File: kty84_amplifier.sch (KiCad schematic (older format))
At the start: 0 parts

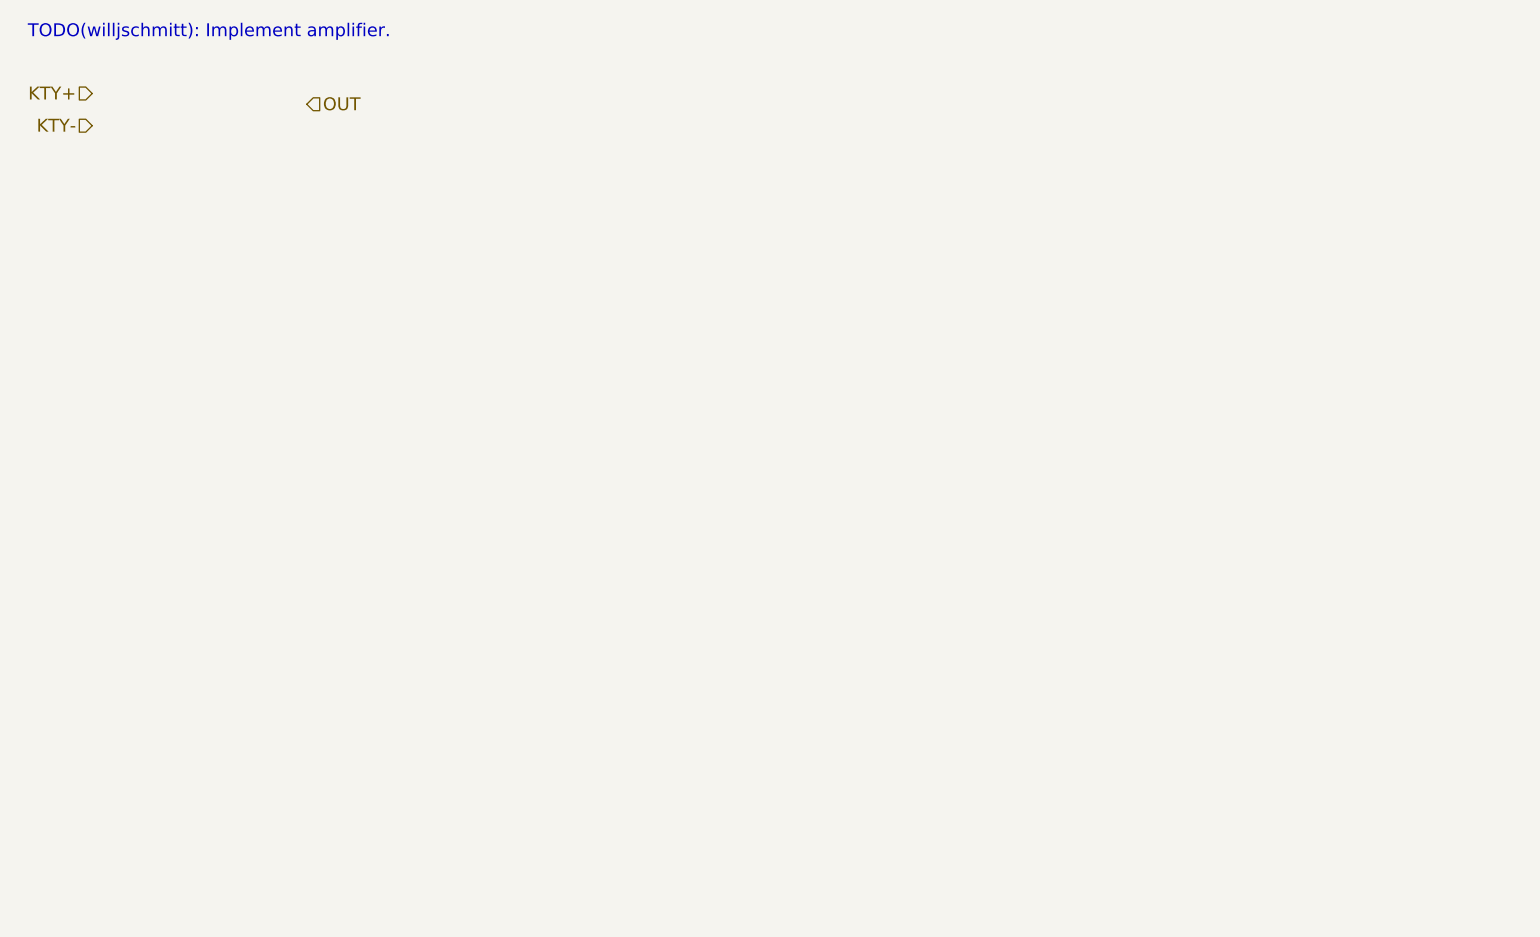
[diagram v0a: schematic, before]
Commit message: Implement temperature sensor amplifier.
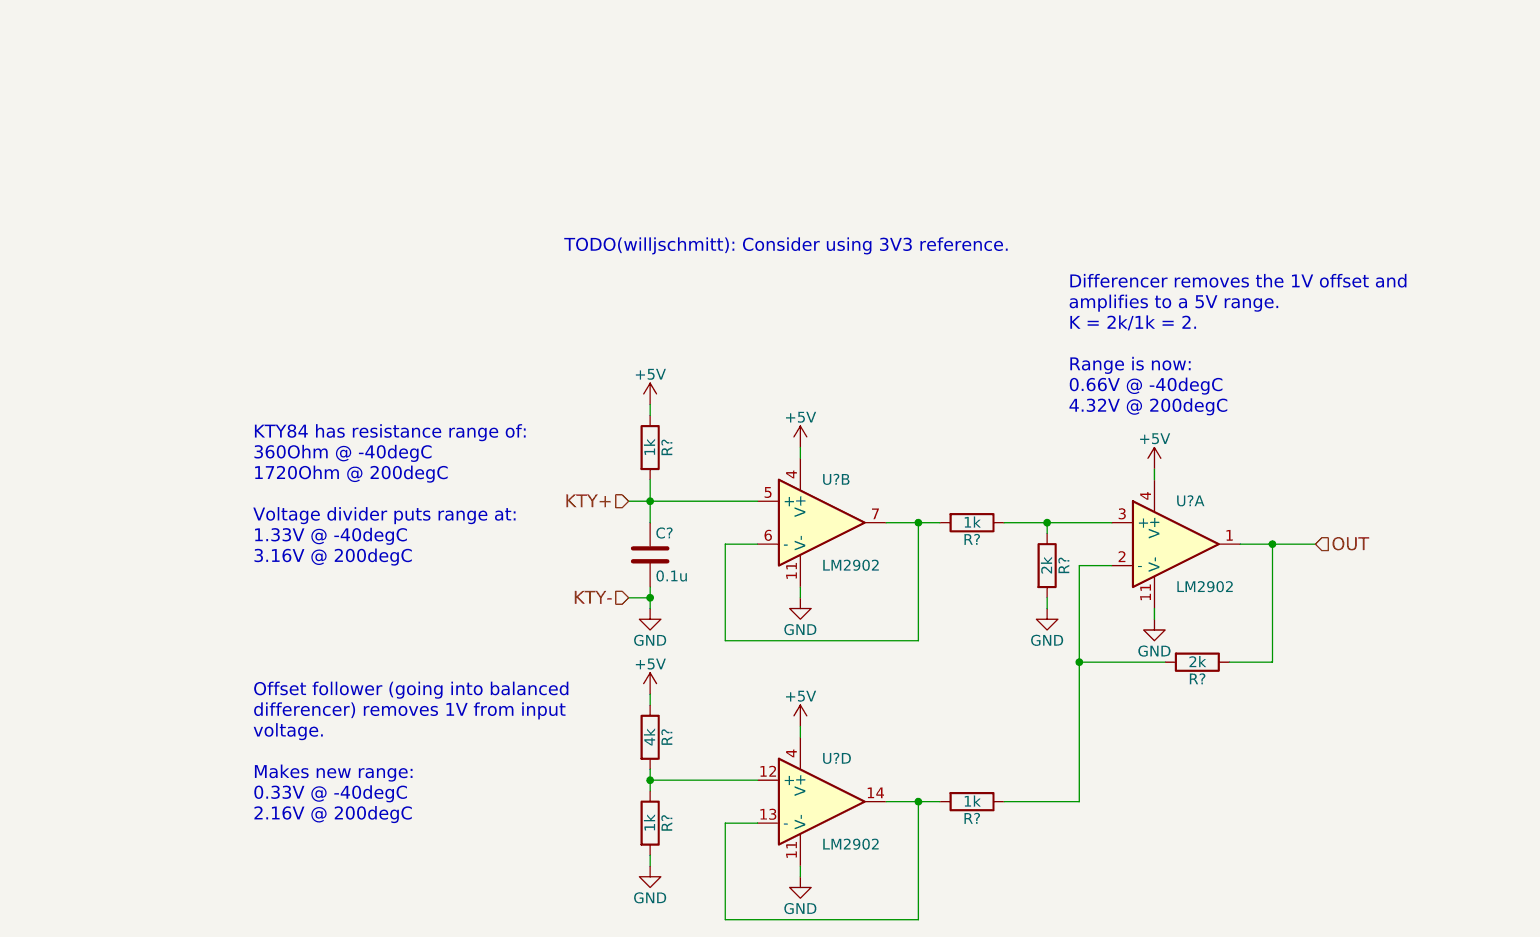
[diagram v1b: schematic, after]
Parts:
- added C?: 0.1u, symbol C
- added R? (x4): 1k, symbol R
- added R?: 4k, symbol R
- added R? (x2): 2k, symbol R
- added U? (x3): LM2902, symbol LM2902
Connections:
- net KTY+: now also C?.1, R?.2, U?.5 (+)
- net OUT: now also R?.1, U?.1
- new net: R?.1, R?.2, U?.2 (-)
- new net: R?.1, R?.1, U?.3 (+)
- new net: R?.2, U?.6 (-), U?.7
- new net: R?.1, R?.2, U?.12 (+)
- new net: R?.2, U?.13 (-), U?.14
- new net +5V: R?.1, R?.1, U?.4 (V+), U?.4 (V+), U?.4 (V+)
- new net GND: C?.2, R?.2, R?.2, U?.11 (V-), U?.11 (V-), U?.11 (V-)
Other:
- note added: "Differencer removes the 1V offset and\namplifies to a 5V range.\nK = 2k/1k = 2.\n\nRange is now:\n0.66V @ -40degC\n4.32V @ 200degC"
- note added: "KTY84 has resistance range of:\n360Ohm @ -40degC\n1720Ohm @ 200degC\n\nVoltage divider puts range at:\n1.33V @ -40degC\n3.16V @ 200degC"
- note added: "Offset follower (going into balanced\ndifferencer) removes 1V from input\nvoltage.\n\nMakes new range:\n0.33V @ -40degC\n2.16V @ 200degC\n"
- note added: "TODO(willjschmitt): Consider using 3V3 reference."
- note removed: "TODO(willjschmitt): Implement amplifier."

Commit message: Annotate and add negative IOC faults.
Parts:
- gave numbers to parts that had none: 9
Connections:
- net KTY+: now also U9.12 (+); no longer U9.5 (+)
- net OUT: now also U9.7; no longer U9.1
- net at R13.1, R15.2: now also U9.6 (-); no longer U9.2 (-)
- net at R12.1, R14.1: now also U9.5 (+); no longer U9.3 (+)
- net at R10.2, R11.1: now also U9.3 (+); no longer U9.12 (+)
- new net: R12.2, U9.13 (-), U9.14
- new net: R13.2, U9.1, U9.2 (-)
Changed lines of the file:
@@
 TODO(willjschmitt): Consider using 3V3 reference.
 $Comp
-L LM2902 U?
-U 1 1 5B0174FE
+L LM2902 U9
+U 2 1 5B0174FE
 P 7200 3400
-F 0 "U?" H 7200 3600 50  0000 L CNN
+AR Path="/5AF6F00C/5B0174FE" Ref="U9"  Part="3"
+AR Path="/5AF71A27/5B0174FE" Ref="U10"  Part="2"
+F 0 "U10" H 7200 3600 50  0000 L CNN
 F 1 "LM2902" H 7200 3200 50  0000 L CNN
 F 2 "" H 7150 3500 50  0001 C CNN
 F 3 "" H 7250 3600 50  0001 C CNN
-	1    7200 3400
-	1    0    0    -1
-$EndComp
-$Comp
-L R R?
+	2    7200 3400
+	1    0    0    -1
+$EndComp
+$Comp
+L R R9
 U 1 1 5B017561
 P 4750 2950
-F 0 "R?" V 4830 2950 50  0000 C CNN
+AR Path="/5AF6F00C/5B017561" Ref="R9"  Part="1"
+AR Path="/5AF71A27/5B017561" Ref="R16"  Part="1"
+F 0 "R16" V 4830 2950 50  0000 C CNN
 F 1 "1k" V 4750 2950 50  0000 C CNN
 F 2 "" V 4680 2950 50  0001 C CNN
@@
 $EndComp
 $Comp
-L C C?
+L C C9
 U 1 1 5B01759E
 P 4750 3450
-F 0 "C?" H 4775 3550 50  0000 L CNN
+AR Path="/5AF6F00C/5B01759E" Ref="C9"  Part="1"
+AR Path="/5AF71A27/5B01759E" Ref="C10"  Part="1"
+F 0 "C10" H 4775 3550 50  0000 L CNN
 F 1 "0.1u" H 4775 3350 50  0000 L CNN
 F 2 "" H 4788 3300 50  0001 C CNN
@@
 $EndComp
 $Comp
-L LM2902 U?
-U 2 1 5B017704
+L LM2902 U9
+U 4 1 5B017704
 P 5550 3300
-F 0 "U?" H 5550 3500 50  0000 L CNN
+AR Path="/5AF6F00C/5B017704" Ref="U9"  Part="1"
+AR Path="/5AF71A27/5B017704" Ref="U9"  Part="4"
+F 0 "U9" H 5550 3500 50  0000 L CNN
 F 1 "LM2902" H 5550 3100 50  0000 L CNN
 F 2 "" H 5500 3400 50  0001 C CNN
 F 3 "" H 5600 3500 50  0001 C CNN
-	2    5550 3300
-	1    0    0    -1
-$EndComp
-$Comp
-L LM2902 U?
-U 4 1 5B01779A
+	4    5550 3300
+	1    0    0    -1
+$EndComp
+$Comp
+L LM2902 U9
+U 1 1 5B01779A
 P 5550 4600
-F 0 "U?" H 5550 4800 50  0000 L CNN
+AR Path="/5AF6F00C/5B01779A" Ref="U9"  Part="2"
+AR Path="/5AF71A27/5B01779A" Ref="U10"  Part="1"
+F 0 "U10" H 5550 4800 50  0000 L CNN
 F 1 "LM2902" H 5550 4400 50  0000 L CNN
 F 2 "" H 5500 4700 50  0001 C CNN
 F 3 "" H 5600 4800 50  0001 C CNN
-	4    5550 4600
+	1    5550 4600
 	1    0    0    -1
 $EndComp
@@
 	5100 4700 5250 4700
 $Comp
-L R R?
+L R R10
 U 1 1 5B017B38
 P 4750 4300
-F 0 "R?" V 4830 4300 50  0000 C CNN
+AR Path="/5AF6F00C/5B017B38" Ref="R10"  Part="1"
+AR Path="/5AF71A27/5B017B38" Ref="R17"  Part="1"
+F 0 "R17" V 4830 4300 50  0000 C CNN
 F 1 "4k" V 4750 4300 50  0000 C CNN
 F 2 "" V 4680 4300 50  0001 C CNN
@@
 $EndComp
 $Comp
-L R R?
+L R R11
 U 1 1 5B017B7D
 P 4750 4700
-F 0 "R?" V 4830 4700 50  0000 C CNN
+AR Path="/5AF6F00C/5B017B7D" Ref="R11"  Part="1"
+AR Path="/5AF71A27/5B017B7D" Ref="R18"  Part="1"
+F 0 "R18" V 4830 4700 50  0000 C CNN
 F 1 "1k" V 4750 4700 50  0000 C CNN
 F 2 "" V 4680 4700 50  0001 C CNN
@@
 Connection ~ 4750 4500
 $Comp
-L GND #PWR?
+L GND #PWR54
 U 1 1 5B017EE0
 P 4750 4900
-F 0 "#PWR?" H 4750 4650 50  0001 C CNN
+AR Path="/5AF6F00C/5B017EE0" Ref="#PWR54"  Part="1"
+AR Path="/5AF71A27/5B017EE0" Ref="#PWR65"  Part="1"
+F 0 "#PWR65" H 4750 4650 50  0001 C CNN
 F 1 "GND" H 4750 4750 50  0000 C CNN
 F 2 "" H 4750 4900 50  0001 C CNN
@@
 	4750 4100 4750 4150
 $Comp
-L +5V #PWR?
+L +5V #PWR53
 U 1 1 5B019FF3
 P 4750 4100
-F 0 "#PWR?" H 4750 3950 50  0001 C CNN
+AR Path="/5AF6F00C/5B019FF3" Ref="#PWR53"  Part="1"
+AR Path="/5AF71A27/5B019FF3" Ref="#PWR64"  Part="1"
+F 0 "#PWR64" H 4750 3950 50  0001 C CNN
 F 1 "+5V" H 4750 4240 50  0000 C CNN
 F 2 "" H 4750 4100 50  0001 C CNN
@@
 $EndComp
 $Comp
-L GND #PWR?
+L GND #PWR52
 U 1 1 5B01A29C
 P 4750 3700
-F 0 "#PWR?" H 4750 3450 50  0001 C CNN
+AR Path="/5AF6F00C/5B01A29C" Ref="#PWR52"  Part="1"
+AR Path="/5AF71A27/5B01A29C" Ref="#PWR63"  Part="1"
+F 0 "#PWR63" H 4750 3450 50  0001 C CNN
 F 1 "GND" H 4750 3550 50  0000 C CNN
 F 2 "" H 4750 3700 50  0001 C CNN
@@
 Connection ~ 4750 3200
 $Comp
-L +5V #PWR?
+L +5V #PWR51
 U 1 1 5B01AA0B
 P 4750 2750
-F 0 "#PWR?" H 4750 2600 50  0001 C CNN
+AR Path="/5AF6F00C/5B01AA0B" Ref="#PWR51"  Part="1"
+AR Path="/5AF71A27/5B01AA0B" Ref="#PWR62"  Part="1"
+F 0 "#PWR62" H 4750 2600 50  0001 C CNN
 F 1 "+5V" H 4750 2890 50  0000 C CNN
 F 2 "" H 4750 2750 50  0001 C CNN
@@
 $EndComp
 $Comp
-L +5V #PWR?
+L +5V #PWR55
 U 1 1 5B01AA2F
 P 5450 2950
-F 0 "#PWR?" H 5450 2800 50  0001 C CNN
+AR Path="/5AF6F00C/5B01AA2F" Ref="#PWR55"  Part="1"
+AR Path="/5AF71A27/5B01AA2F" Ref="#PWR66"  Part="1"
+F 0 "#PWR66" H 5450 2800 50  0001 C CNN
 F 1 "+5V" H 5450 3090 50  0000 C CNN
 F 2 "" H 5450 2950 50  0001 C CNN
@@
 	5100 3400 5250 3400
 $Comp
-L R R?
+L R R12
 U 1 1 5B01AF09
 P 6250 3300
-F 0 "R?" V 6330 3300 50  0000 C CNN
+AR Path="/5AF6F00C/5B01AF09" Ref="R12"  Part="1"
+AR Path="/5AF71A27/5B01AF09" Ref="R19"  Part="1"
+F 0 "R19" V 6330 3300 50  0000 C CNN
 F 1 "1k" V 6250 3300 50  0000 C CNN
 F 2 "" V 6180 3300 50  0001 C CNN
@@
 Connection ~ 6000 3300
 $Comp
-L R R?
+L R R14
 U 1 1 5B01AFB1
 P 6600 3500
-F 0 "R?" V 6680 3500 50  0000 C CNN
+AR Path="/5AF6F00C/5B01AFB1" Ref="R14"  Part="1"
+AR Path="/5AF71A27/5B01AFB1" Ref="R21"  Part="1"
+F 0 "R21" V 6680 3500 50  0000 C CNN
 F 1 "2k" V 6600 3500 50  0000 C CNN
 F 2 "" V 6530 3500 50  0001 C CNN
@@
 $EndComp
 $Comp
-L R R?
+L R R15
 U 1 1 5B01B166
 P 7300 3950
-F 0 "R?" V 7380 3950 50  0000 C CNN
+AR Path="/5AF6F00C/5B01B166" Ref="R15"  Part="1"
+AR Path="/5AF71A27/5B01B166" Ref="R22"  Part="1"
+F 0 "R22" V 7380 3950 50  0000 C CNN
 F 1 "2k" V 7300 3950 50  0000 C CNN
 F 2 "" V 7230 3950 50  0001 C CNN
@@
 $EndComp
 $Comp
-L R R?
+L R R13
 U 1 1 5B01B319
 P 6250 4600
-F 0 "R?" V 6330 4600 50  0000 C CNN
+AR Path="/5AF6F00C/5B01B319" Ref="R13"  Part="1"
+AR Path="/5AF71A27/5B01B319" Ref="R20"  Part="1"
+F 0 "R20" V 6330 4600 50  0000 C CNN
 F 1 "1k" V 6250 4600 50  0000 C CNN
 F 2 "" V 6180 4600 50  0001 C CNN
@@
 Connection ~ 7650 3400
 $Comp
-L +5V #PWR?
+L +5V #PWR60
 U 1 1 5B01C1FC
 P 7100 3050
-F 0 "#PWR?" H 7100 2900 50  0001 C CNN
+AR Path="/5AF6F00C/5B01C1FC" Ref="#PWR60"  Part="1"
+AR Path="/5AF71A27/5B01C1FC" Ref="#PWR71"  Part="1"
+F 0 "#PWR71" H 7100 2900 50  0001 C CNN
 F 1 "+5V" H 7100 3190 50  0000 C CNN
 F 2 "" H 7100 3050 50  0001 C CNN
@@
 $EndComp
 $Comp
-L +5V #PWR?
+L +5V #PWR57
 U 1 1 5B01C230
 P 5450 4250
-F 0 "#PWR?" H 5450 4100 50  0001 C CNN
+AR Path="/5AF6F00C/5B01C230" Ref="#PWR57"  Part="1"
+AR Path="/5AF71A27/5B01C230" Ref="#PWR68"  Part="1"
+F 0 "#PWR68" H 5450 4100 50  0001 C CNN
 F 1 "+5V" H 5450 4390 50  0000 C CNN
 F 2 "" H 5450 4250 50  0001 C CNN
@@
 	7100 3050 7100 3100
 $Comp
-L GND #PWR?
+L GND #PWR56
 U 1 1 5B01C46A
 P 5450 3650
-F 0 "#PWR?" H 5450 3400 50  0001 C CNN
+AR Path="/5AF6F00C/5B01C46A" Ref="#PWR56"  Part="1"
+AR Path="/5AF71A27/5B01C46A" Ref="#PWR67"  Part="1"
+F 0 "#PWR67" H 5450 3400 50  0001 C CNN
 F 1 "GND" H 5450 3500 50  0000 C CNN
 F 2 "" H 5450 3650 50  0001 C CNN
@@
 	5450 3600 5450 3650
 $Comp
-L GND #PWR?
+L GND #PWR61
 U 1 1 5B01C692
 P 7100 3750
-F 0 "#PWR?" H 7100 3500 50  0001 C CNN
+AR Path="/5AF6F00C/5B01C692" Ref="#PWR61"  Part="1"
+AR Path="/5AF71A27/5B01C692" Ref="#PWR72"  Part="1"
+F 0 "#PWR72" H 7100 3500 50  0001 C CNN
 F 1 "GND" H 7100 3600 50  0000 C CNN
 F 2 "" H 7100 3750 50  0001 C CNN
@@
 $EndComp
 $Comp
-L GND #PWR?
+L GND #PWR58
 U 1 1 5B01C72D
 P 5450 4950
-F 0 "#PWR?" H 5450 4700 50  0001 C CNN
+AR Path="/5AF6F00C/5B01C72D" Ref="#PWR58"  Part="1"
+AR Path="/5AF71A27/5B01C72D" Ref="#PWR69"  Part="1"
+F 0 "#PWR69" H 5450 4700 50  0001 C CNN
 F 1 "GND" H 5450 4800 50  0000 C CNN
 F 2 "" H 5450 4950 50  0001 C CNN
@@
 Differencer removes the 1V offset and\namplifies to a 5V range.\nK = 2k/1k = 2.\n\nRange is now:\n0.66V @ -40degC\n4.32V @ 200degC
 $Comp
-L GND #PWR?
+L GND #PWR59
 U 1 1 5B01E4A0
 P 6600 3700
-F 0 "#PWR?" H 6600 3450 50  0001 C CNN
+AR Path="/5AF6F00C/5B01E4A0" Ref="#PWR59"  Part="1"
+AR Path="/5AF71A27/5B01E4A0" Ref="#PWR70"  Part="1"
+F 0 "#PWR70" H 6600 3450 50  0001 C CNN
 F 1 "GND" H 6600 3550 50  0000 C CNN
 F 2 "" H 6600 3700 50  0001 C CNN
